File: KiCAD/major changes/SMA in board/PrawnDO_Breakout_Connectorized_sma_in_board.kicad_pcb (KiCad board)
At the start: 2 copper layers, 113 x 86.8 mm, 83 parts, among them IC1 74LVT245D,118, IC2 74LVT245D,118, IC3 74LVT245D,118, IC4 74LVT245D,118, J1 do15, J10 do6, J11 do5, J12 do4, J13 do3, J14 do2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

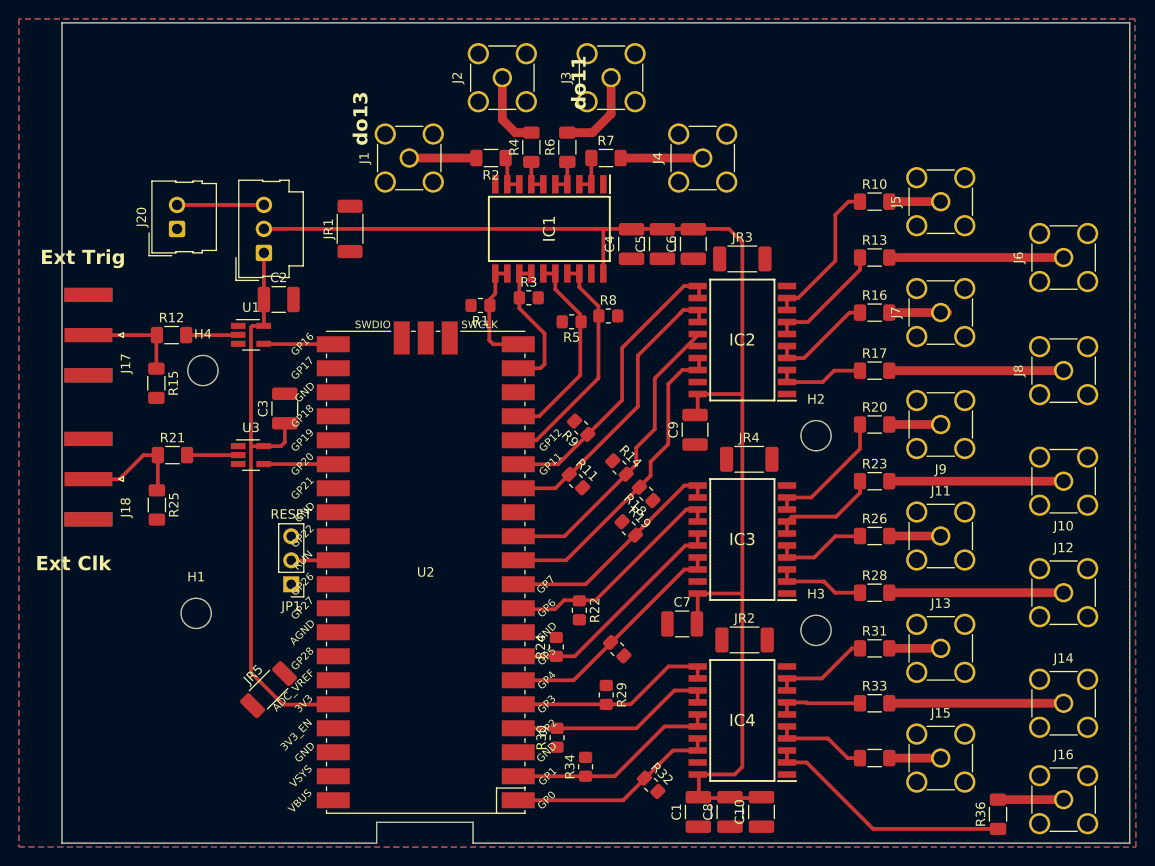
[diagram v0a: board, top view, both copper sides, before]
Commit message: Satisfied DRC
Footprint and unconnected track errors
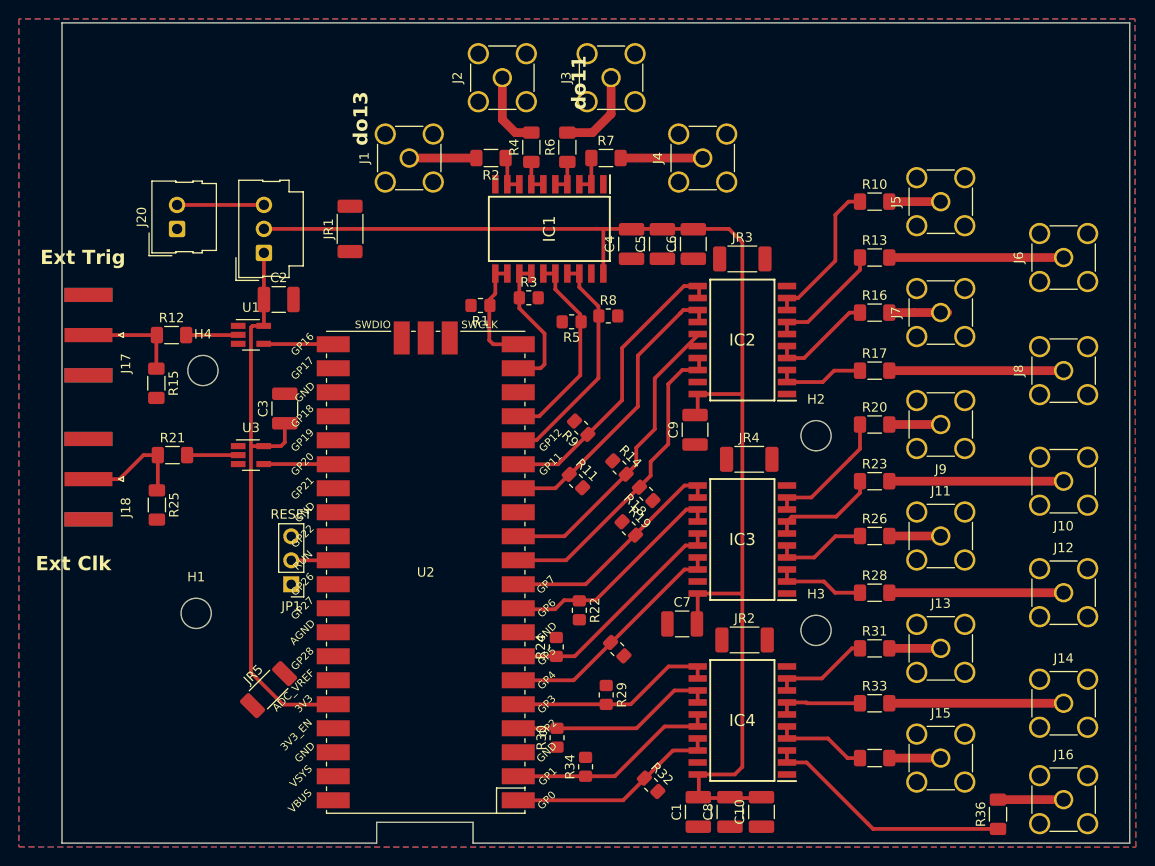
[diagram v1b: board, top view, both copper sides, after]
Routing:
- net Net-(IC1A-B6): track 12.1 -> 10.9 mm
- net Net-(IC1A-A6): track 4.62 -> 4.12 mm
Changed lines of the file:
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@@
   (segment (start 92.073 86.261) (end 91.9 86.434) (width 0.4) (layer "F.Cu") (net 1))
   (segment (start 93.25 86.261) (end 92.073 86.261) (width 0.4) (layer "F.Cu") (net 1))
+  (segment (start 93.25 98.9875) (end 91.9665 98.9875) (width 0.4) (layer "F.Cu") (net 1))
   (segment (start 93.2715 86.2395) (end 93.25 86.261) (width 0.4) (layer "F.Cu") (net 1))
   (segment (start 95.294448 126.3375) (end 91.9 122.943052) (width 0.4) (layer "F.Cu") (net 1))
-  (segment (start 91.9665 98.9875) (end 93.25 98.9875) (width 0.4) (layer "F.Cu") (net 1))
   (segment (start 101.474448 126.3375) (end 95.294448 126.3375) (width 0.4) (layer "F.Cu") (net 1))
   (segment (start 91.9 122.943052) (end 91.9 98.921) (width 0.4) (layer "F.Cu") (net 1))
-  (segment (start 93.296 83.2955) (end 93.2715 83.271) (width 0.4) (layer "F.Cu") (net 1))
-  (segment (start 93.25 98.9875) (end 93.25 98.901) (width 0.4) (layer "F.Cu") (net 1))
   (segment (start 93.2715 78.54) (end 93.2715 86.2395) (width 0.4) (layer "F.Cu") (net 1))
   (segment (start 95.48 96.5715) (end 95.48 98.585) (width 0.4) (layer "F.Cu") (net 1))
   (segment (start 95.48 98.585) (end 95.0775 98.9875) (width 0.4) (layer "F.Cu") (net 1))
-  (segment (start 91.9 98.921) (end 91.9665 98.9875) (width 0.4) (layer "F.Cu") (net 1))
   (segment (start 91.9 86.434) (end 91.9 98.921) (width 0.4) (layer "F.Cu") (net 1))
   (segment (start 101.504448 126.3075) (end 101.474448 126.3375) (width 0.4) (layer "F.Cu") (net 1))
   (segment (start 137.5357 79.139) (end 137.5384 79.1363) (width 0.4) (layer "F.Cu") (net 2))
   (segment (start 159.45 96.7) (end 164.9 96.7) (width 0.93) (layer "F.Cu") (net 3))
-  (segment (start 164.89 96.696) (end 164.9 96.706) (width 0.93) (layer "F.Cu") (net 3))
   (segment (start 170.956 136.398) (end 177.898 136.398) (width 0.93) (layer "F.Cu") (net 4))
   (segment (start 177.898 136.398) (end 177.9 136.4) (width 0.93) (layer "F.Cu") (net 4))
@@
   (segment (start 177.9 114.5) (end 159.45 114.5) (width 0.93) (layer "F.Cu") (net 16))
   (segment (start 159.55 120.39) (end 164.722 120.39) (width 0.93) (layer "F.Cu") (net 17))
-  (segment (start 127.9202 68.5002) (end 127.92 68.5) (width 0.4) (layer "F.Cu") (net 18))
   (segment (start 127.9202 71.275) (end 127.9202 68.5002) (width 0.4) (layer "F.Cu") (net 18))
-  (segment (start 127.92 71.2748) (end 127.9202 71.275) (width 0.4) (layer "F.Cu") (net 18))
   (segment (start 127.9202 71.275) (end 126.6502 71.275) (width 0.4) (layer "F.Cu") (net 18))
-  (segment (start 127.9202 68.4202) (end 127.92 68.42) (width 0.4) (layer "F.Cu") (net 18))
-  (segment (start 126.65 71.2748) (end 126.6502 71.275) (width 0.4) (layer "F.Cu") (net 18))
   (segment (start 101.484448 88.1875) (end 93.3225 88.1875) (width 0.4) (layer "F.Cu") (net 20))
   (segment (start 93.3225 88.1875) (end 93.296 88.161) (width 0.4) (layer "F.Cu") (net 20))
@@
   (segment (start 77.99 102.48) (end 80.5325 99.9375) (width 0.4) (layer "F.Cu") (net 41))
   (segment (start 125.38 68.91) (end 125.38 71.2748) (width 0.4) (layer "F.Cu") (net 42))
-  (segment (start 124.1 71.2648) (end 124.1102 71.275) (width 0.4) (layer "F.Cu") (net 42))
   (segment (start 125.3802 71.275) (end 124.1102 71.275) (width 0.4) (layer "F.Cu") (net 42))
   (segment (start 125.38 71.2748) (end 125.3802 71.275) (width 0.4) (layer "F.Cu") (net 42))
   (segment (start 121.5702 71.275) (end 122.8402 71.275) (width 0.4) (layer "F.Cu") (net 43))
   (segment (start 121.5702 68.9662) (end 121.5702 71.275) (width 0.4) (layer "F.Cu") (net 43))
-  (segment (start 119.0302 68.1772) (end 118.853 68) (width 0.4) (layer "F.Cu") (net 44))
-  (segment (start 118.853 68.1782) (end 119.0308 68.356) (width 0.4) (layer "F.Cu") (net 44))
-  (segment (start 119.0308 71.2744) (end 119.0302 71.275) (width 0.4) (layer "F.Cu") (net 44))
   (segment (start 119.0302 71.275) (end 119.0302 68.6802) (width 0.4) (layer "F.Cu") (net 44))
   (segment (start 119.0302 71.275) (end 120.3002 71.275) (width 0.4) (layer "F.Cu") (net 44))
@@
   (segment (start 119.284448 88.2075) (end 117.5335 88.2075) (width 0.4) (layer "F.Cu") (net 45))
   (segment (start 117.121 87.795) (end 117.121 83.4986) (width 0.4) (layer "F.Cu") (net 45))
-  (segment (start 119.9805 88.2075) (end 120.306 87.882) (width 0.4) (layer "F.Cu") (net 45))
-  (segment (start 119.284448 88.2075) (end 119.9805 88.2075) (width 0.4) (layer "F.Cu") (net 45))
   (segment (start 122.9672 90.3328) (end 122.9672 87.0758) (width 0.4) (layer "F.Cu") (net 46))
   (segment (start 122.5525 90.7475) (end 122.9672 90.3328) (width 0.4) (layer "F.Cu") (net 46))
@@
   (segment (start 122.9672 87.0758) (end 120.3002 84.4088) (width 0.4) (layer "F.Cu") (net 46))
   (segment (start 119.284448 90.7475) (end 122.5525 90.7475) (width 0.4) (layer "F.Cu") (net 46))
-  (segment (start 121.044448 95.8275) (end 119.284448 95.8275) (width 0.4) (layer "F.Cu") (net 47))
+  (segment (start 122.4075 95.8275) (end 119.284448 95.8275) (width 0.4) (layer "F.Cu") (net 47))
   (segment (start 124.1102 82.4022) (end 126.7518 85.0438) (width 0.4) (layer "F.Cu") (net 47))
   (segment (start 124.1102 80.725) (end 124.1102 82.4022) (width 0.4) (layer "F.Cu") (net 47))
   (segment (start 126.7518 85.0438) (end 126.7518 91.4832) (width 0.4) (layer "F.Cu") (net 47))
-  (segment (start 121.044448 95.8275) (end 121.046948 95.83) (width 0.4) (layer "F.Cu") (net 47))
   (segment (start 126.7518 91.4832) (end 122.4075 95.8275) (width 0.4) (layer "F.Cu") (net 47))
   (segment (start 122.8402 80.725) (end 124.1102 80.725) (width 0.4) (layer "F.Cu") (net 47))
-  (segment (start 122.4075 95.8275) (end 121.044448 95.8275) (width 0.4) (layer "F.Cu") (net 47))
   (segment (start 126.6502 82.1736) (end 128.6728 84.1962) (width 0.4) (layer "F.Cu") (net 48))
   (segment (start 128.6728 84.1962) (end 128.6728 91.7992) (width 0.4) (layer "F.Cu") (net 48))
@@
   (segment (start 139.175 109.504) (end 137.877 109.504) (width 0.4) (layer "F.Cu") (net 63))
   (segment (start 126.1535 121.2275) (end 119.284448 121.2275) (width 0.4) (layer "F.Cu") (net 63))
-  (segment (start 119.284448 121.2275) (end 119.545948 120.966) (width 0.4) (layer "F.Cu") (net 63))
   (segment (start 137.877 109.504) (end 126.1535 121.2275) (width 0.4) (layer "F.Cu") (net 63))
   (segment (start 126.0519 123.7675) (end 119.284448 123.7675) (width 0.4) (layer "F.Cu") (net 64))
@@
   (segment (start 150.762 126.2) (end 156.35 126.2) (width 0.4) (layer "F.Cu") (net 67))
   (segment (start 148.6218 124.8456) (end 148.6218 123.5756) (width 0.4) (layer "F.Cu") (net 68))
-  (segment (start 156.4424 120.7816) (end 156.45 120.774) (width 0.4) (layer "F.Cu") (net 68))
   (segment (start 152.3084 123.5756) (end 148.625 123.5756) (width 0.4) (layer "F.Cu") (net 68))
   (segment (start 156.45 120.39) (end 155.494 120.39) (width 0.4) (layer "F.Cu") (net 68))
   (segment (start 155.494 120.39) (end 152.3084 123.5756) (width 0.4) (layer "F.Cu") (net 68))
   (segment (start 139.1718 123.5756) (end 139.1718 122.3056) (width 0.4) (layer "F.Cu") (net 69))
-  (segment (start 119.331948 126.26) (end 119.284448 126.3075) (width 0.4) (layer "F.Cu") (net 69))
   (segment (start 139.175 122.3056) (end 136.0877 122.3056) (width 0.4) (layer "F.Cu") (net 69))
   (segment (start 119.284448 126.3075) (end 132.0858 126.3075) (width 0.4) (layer "F.Cu") (net 69))
@@
   (segment (start 131.2843 136.4675) (end 136.5054 131.2464) (width 0.4) (layer "F.Cu") (net 72))
   (segment (start 119.284448 136.4675) (end 131.2843 136.4675) (width 0.4) (layer "F.Cu") (net 72))
-  (segment (start 90.596 87.211) (end 90.5695 87.2375) (width 0.4) (layer "F.Cu") (net 73))
   (segment (start 90.5695 87.2375) (end 85.044448 87.2375) (width 0.4) (layer "F.Cu") (net 73))
   (segment (start 90.55 99.9375) (end 85.144448 99.9375) (width 0.4) (layer "F.Cu") (net 74))
